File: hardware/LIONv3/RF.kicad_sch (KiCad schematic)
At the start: 17 parts, among them U5 E80-900M2213S, U6 INA226AIDGSR, U7 XL-1608UBC-04, U8 W25Q16JVSSIQTR

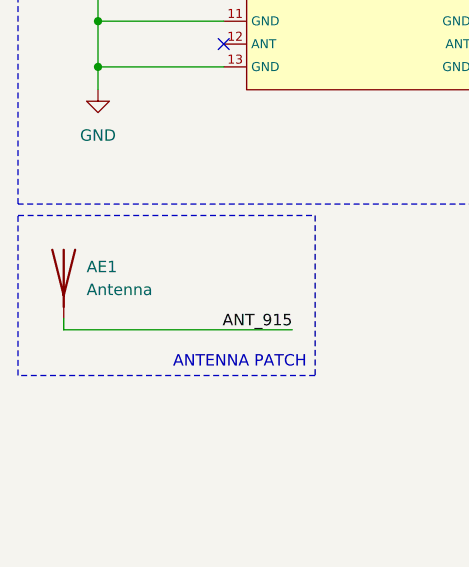
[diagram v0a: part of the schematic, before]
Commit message: feat(hardware): organize repo structure
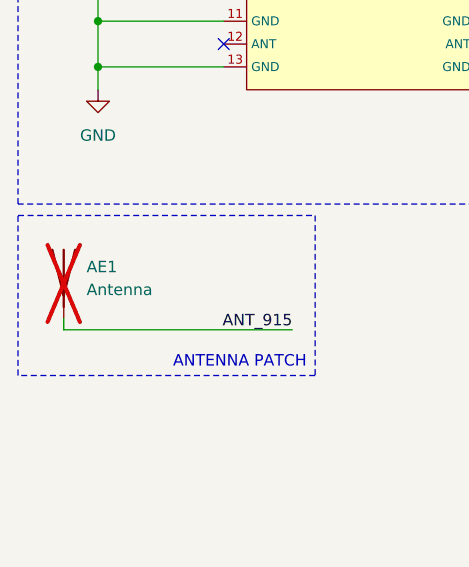
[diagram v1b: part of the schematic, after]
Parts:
- AE1: now not fitted
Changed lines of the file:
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@@
 		(unit 1)
 		(body_style 1)
-		(exclude_from_sim no)
+		(exclude_from_sim yes)
 		(in_bom no)
-		(on_board yes)
+		(on_board no)
 		(in_pos_files no)
-		(dnp no)
+		(dnp yes)
 		(fields_autoplaced yes)
 		(property "Reference" "AE1"

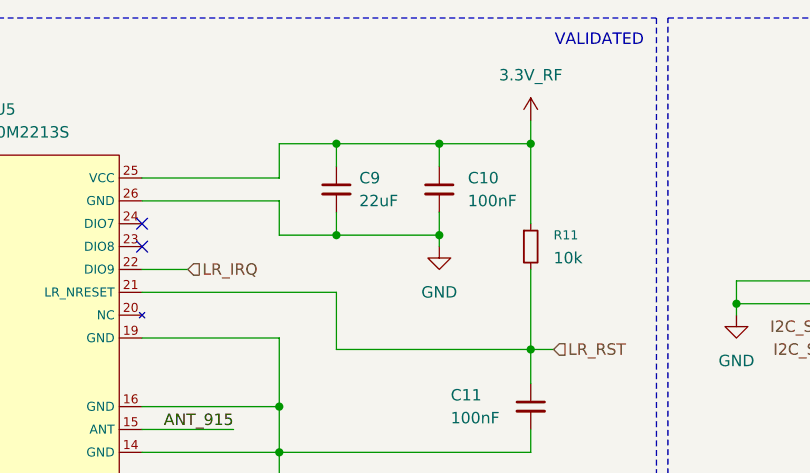
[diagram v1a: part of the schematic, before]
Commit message: Add TVS diode protection (ESD9B3.3ST5G)
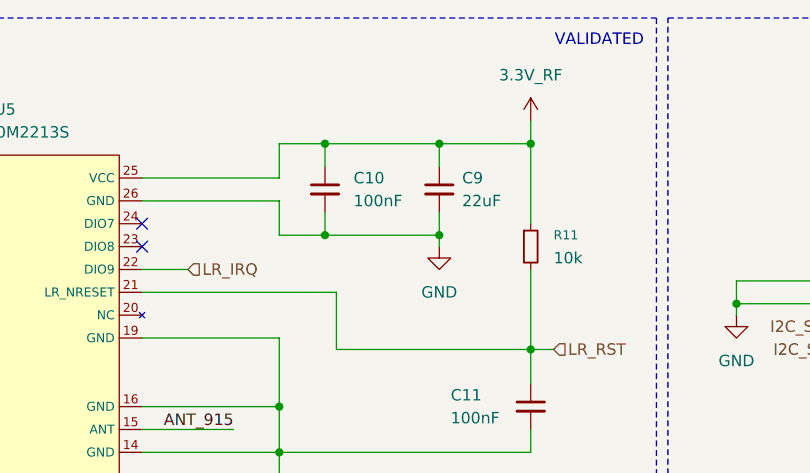
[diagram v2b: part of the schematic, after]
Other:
- moved on the sheet: C10, C9
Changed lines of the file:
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@@
 	)
 	(junction
-		(at 88.9 27.94)
-		(diameter 0)
-		(color 0 0 0 0)
-	)
-	(junction
 		(at 110.49 27.94)
 		(diameter 0)
@@
 	)
 	(junction
-		(at 88.9 38.1)
+		(at 87.63 27.94)
 		(diameter 0)
 		(color 0 0 0 0)
@@
 	)
 	(junction
-		(at 22.86 52.07)
+		(at 100.33 27.94)
 		(diameter 0)
 		(color 0 0 0 0)
 	)
 	(junction
-		(at 82.55 62.23)
+		(at 22.86 52.07)
 		(diameter 0)
 		(color 0 0 0 0)
 	)
 	(junction
-		(at 110.49 50.8)
+		(at 82.55 62.23)
 		(diameter 0)
 		(color 0 0 0 0)
 	)
 	(junction
-		(at 31.75 34.29)
+		(at 110.49 50.8)
 		(diameter 0)
 		(color 0 0 0 0)
 	)
 	(junction
-		(at 100.33 27.94)
+		(at 31.75 34.29)
 		(diameter 0)
 		(color 0 0 0 0)
@@
 	)
 	(junction
-		(at 182.88 33.02)
+		(at 87.63 38.1)
 		(diameter 0)
 		(color 0 0 0 0)
 	)
 	(junction
-		(at 22.86 57.15)
+		(at 182.88 33.02)
 		(diameter 0)
 		(color 0 0 0 0)
 	)
 	(junction
-		(at 100.33 38.1)
+		(at 22.86 57.15)
 		(diameter 0)
 		(color 0 0 0 0)
@@
 	)
 	(junction
+		(at 100.33 38.1)
+		(diameter 0)
+		(color 0 0 0 0)
+	)
+	(junction
 		(at 82.55 57.15)
 		(diameter 0)
@@
 	(wire
 		(pts
-			(xy 88.9 27.94) (xy 88.9 30.48)
+			(xy 100.33 27.94) (xy 100.33 30.48)
 		)
 		(stroke
@@
 	(wire
 		(pts
-			(xy 82.55 57.15) (xy 82.55 62.23)
+			(xy 87.63 38.1) (xy 100.33 38.1)
 		)
 		(stroke
@@
 	(wire
 		(pts
-			(xy 100.33 30.48) (xy 100.33 27.94)
+			(xy 82.55 57.15) (xy 82.55 62.23)
 		)
 		(stroke
@@
 	(wire
 		(pts
-			(xy 22.86 52.07) (xy 36.83 52.07)
+			(xy 87.63 30.48) (xy 87.63 27.94)
 		)
 		(stroke
@@
 	(wire
 		(pts
-			(xy 29.21 41.91) (xy 36.83 41.91)
+			(xy 22.86 52.07) (xy 36.83 52.07)
 		)
 		(stroke
@@
 	(wire
 		(pts
-			(xy 100.33 38.1) (xy 88.9 38.1)
+			(xy 29.21 41.91) (xy 36.83 41.91)
 		)
 		(stroke
@@
 	(wire
 		(pts
-			(xy 88.9 35.56) (xy 88.9 38.1)
+			(xy 100.33 35.56) (xy 100.33 38.1)
 		)
 		(stroke
@@
 	(wire
 		(pts
+			(xy 87.63 27.94) (xy 100.33 27.94)
+		)
+		(stroke
+			(width 0)
+			(type default)
+		)
+	)
+	(wire
+		(pts
 			(xy 67.31 49.53) (xy 82.55 49.53)
 		)
@@
 	(wire
 		(pts
-			(xy 82.55 27.94) (xy 110.49 27.94)
+			(xy 82.55 27.94) (xy 87.63 27.94)
 		)
 		(stroke
@@
 	(wire
 		(pts
-			(xy 88.9 38.1) (xy 82.55 38.1)
+			(xy 82.55 38.1) (xy 87.63 38.1)
 		)
 		(stroke
@@
 	(wire
 		(pts
+			(xy 100.33 27.94) (xy 110.49 27.94)
+		)
+		(stroke
+			(width 0)
+			(type default)
+		)
+	)
+	(wire
+		(pts
 			(xy 273.05 107.95) (xy 273.05 109.22)
 		)
@@
 	(wire
 		(pts
-			(xy 100.33 35.56) (xy 100.33 38.1)
+			(xy 87.63 35.56) (xy 87.63 38.1)
 		)
 		(stroke
@@
 	(symbol
 		(lib_id "Device:C_Small")
-		(at 88.9 33.02 0)
+		(at 100.33 33.02 0)
 		(unit 1)
 		(body_style 1)
@@
 		(fields_autoplaced yes)
 		(property "Reference" "C9"
-			(at 91.44 31.7562 0)
+			(at 102.87 31.7562 0)
 			(show_name no)
 			(do_not_autoplace no)
@@
 		)
 		(property "Value" "22uF"
-			(at 91.44 34.2962 0)
+			(at 102.87 34.2962 0)
 			(show_name no)
 			(do_not_autoplace no)
@@
 		)
 		(property "Footprint" "Capacitor_SMD:C_0805_2012Metric"
-			(at 88.9 33.02 0)
+			(at 100.33 33.02 0)
 			(hide yes)
 			(show_name no)
@@
 		)
 		(property "Datasheet" ""
-			(at 88.9 33.02 0)
+			(at 100.33 33.02 0)
 			(hide yes)
 			(show_name no)
@@
 		)
 		(property "Description" "Unpolarized capacitor, small symbol"
-			(at 88.9 33.02 0)
+			(at 100.33 33.02 0)
 			(hide yes)
 			(show_name no)
@@
 		)
 		(property "LCSC" "C45783"
-			(at 88.9 33.02 0)
+			(at 100.33 33.02 0)
 			(hide yes)
 			(show_name no)
@@
 	(symbol
 		(lib_id "Device:C_Small")
-		(at 100.33 33.02 0)
+		(at 87.63 33.02 0)
 		(unit 1)
 		(body_style 1)
@@
 		(fields_autoplaced yes)
 		(property "Reference" "C10"
-			(at 103.505 31.7562 0)
+			(at 90.805 31.7562 0)
 			(show_name no)
 			(do_not_autoplace no)
@@
 		)
 		(property "Value" "100nF"
-			(at 103.505 34.2962 0)
+			(at 90.805 34.2962 0)
 			(show_name no)
 			(do_not_autoplace no)
@@
 		)
 		(property "Footprint" "Capacitor_SMD:C_0402_1005Metric"
-			(at 100.33 33.02 0)
+			(at 87.63 33.02 0)
 			(hide yes)
 			(show_name no)
@@
 		)
 		(property "Datasheet" ""
-			(at 100.33 33.02 0)
+			(at 87.63 33.02 0)
 			(hide yes)
 			(show_name no)
@@
 		)
 		(property "Description" "Unpolarized capacitor, small symbol"
-			(at 100.33 33.02 0)
+			(at 87.63 33.02 0)
 			(hide yes)
 			(show_name no)
@@
 		)
 		(property "LCSC" "C307331"
-			(at 100.33 33.02 0)
+			(at 87.63 33.02 0)
 			(hide yes)
 			(show_name no)

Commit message: feat(hardware): improves LED series currents
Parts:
- R14: value 68 -> 1k
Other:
- note added: "BLUE RX/TX@3.4mA"
- note removed: "BLUE RX/TX"
- note removed: "VALIDATED"
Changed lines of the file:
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@@
 		(comment 3 "2026-08-12")
 	)
-	(text "BLUE RX/TX\n"
+	(text "BLUE RX/TX@3.4mA"
 		(exclude_from_sim no)
 		(at 236.22 43.18 0)
@@
 		)
 	)
-	(text "VALIDATED"
-		(exclude_from_sim no)
-		(at 118.11 16.51 0)
-		(effects
-			(font
-				(size 1.27 1.27)
-			)
-		)
-	)
-	(text "VALIDATED"
-		(exclude_from_sim no)
-		(at 276.86 81.28 0)
-		(effects
-			(font
-				(size 1.27 1.27)
-			)
-		)
-	)
-	(text "VALIDATED"
-		(exclude_from_sim no)
-		(at 204.47 16.51 0)
-		(effects
-			(font
-				(size 1.27 1.27)
-			)
-		)
-	)
-	(text "VALIDATED"
-		(exclude_from_sim no)
-		(at 276.86 16.51 0)
-		(effects
-			(font
-				(size 1.27 1.27)
-			)
-		)
-	)
 	(text_box "MEMORY"
 		(exclude_from_sim no)
@@
 			)
 		)
-		(property "Value" "68"
+		(property "Value" "1k"
 			(at 251.46 35.56 90)
 			(show_name no)
@@
 			)
 		)
-		(property "Datasheet" "https://atta.szlcsc.com/upload/public/pdf/source/20210617/C2837377_50FC585D376FE0CDA016E524346528FF.pdf"
+		(property "Datasheet" "https://www.lcsc.com/datasheet/C965807.pdf"
 			(at 233.934 37.973 0)
 			(hide yes)

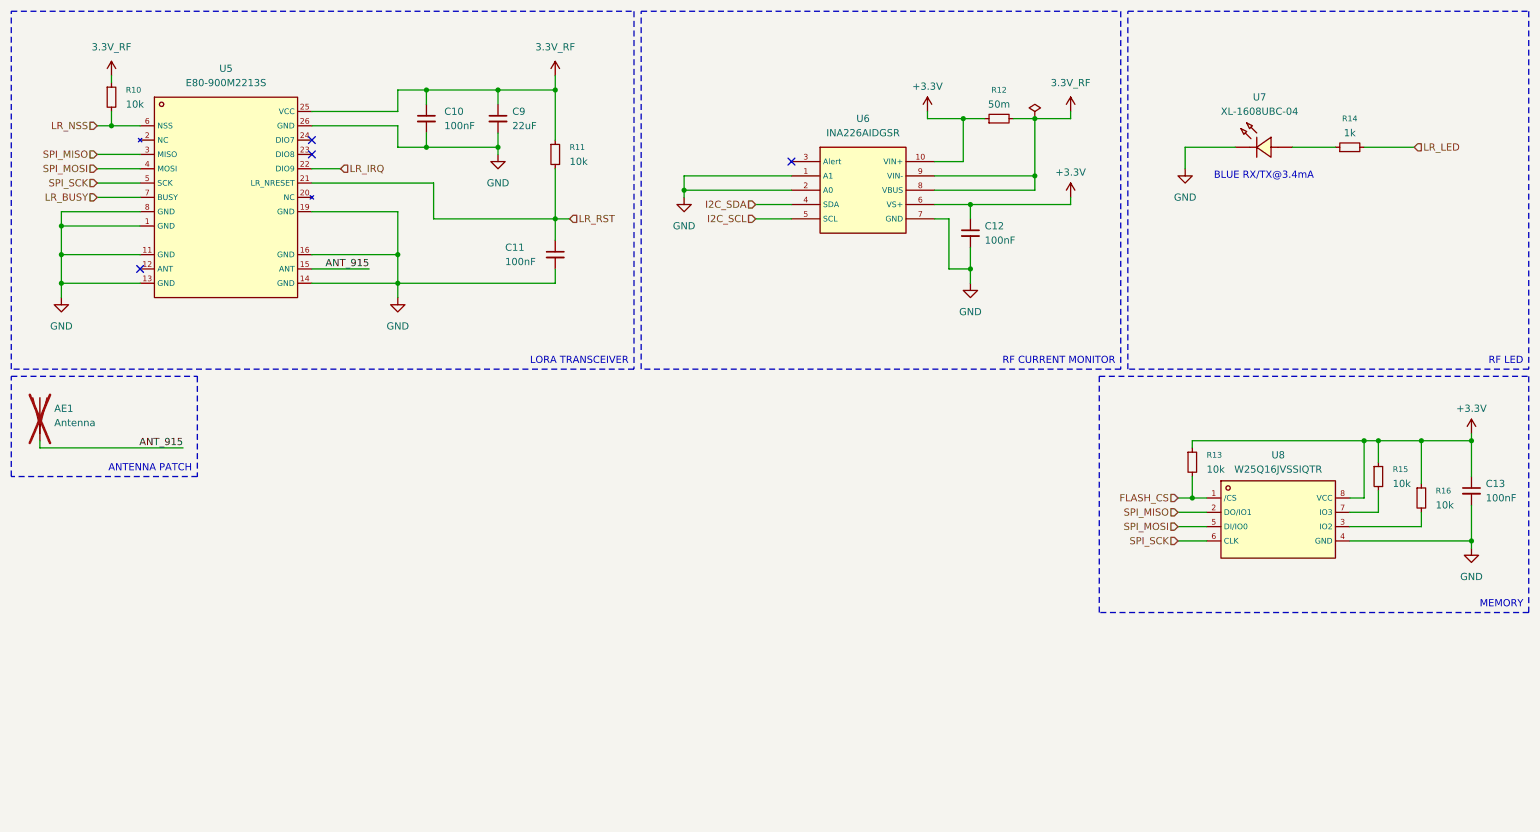
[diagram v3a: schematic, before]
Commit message: feat(hardware): change SPI terminology (new OSHWA naming conventions)
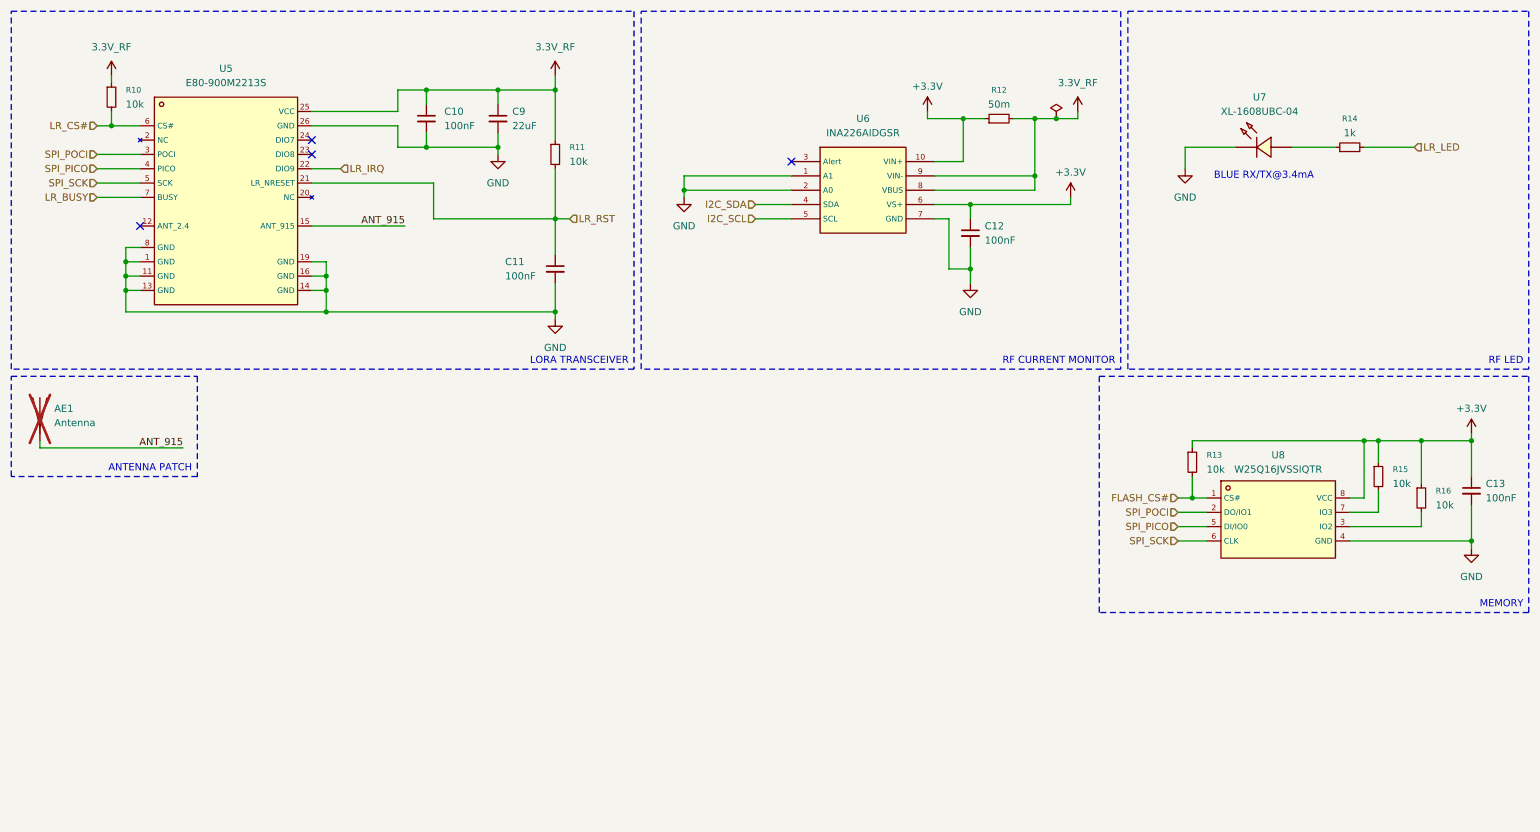
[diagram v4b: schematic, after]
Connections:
- net FLASH_CS renamed FLASH_CS#
- net LR_NSS renamed LR_CS#
- net SPI_MISO renamed SPI_POCI
- net SPI_MOSI renamed SPI_PICO
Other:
- moved on the sheet: C11, U5

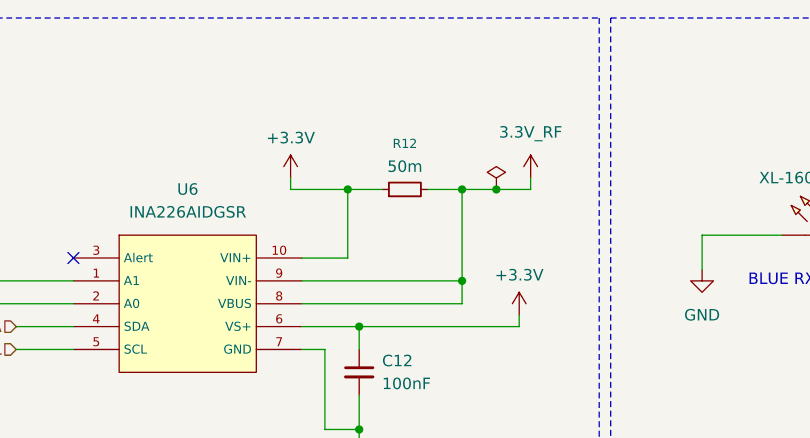
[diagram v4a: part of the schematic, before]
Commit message: feat(hardware): add shunt resistor rating to schematic
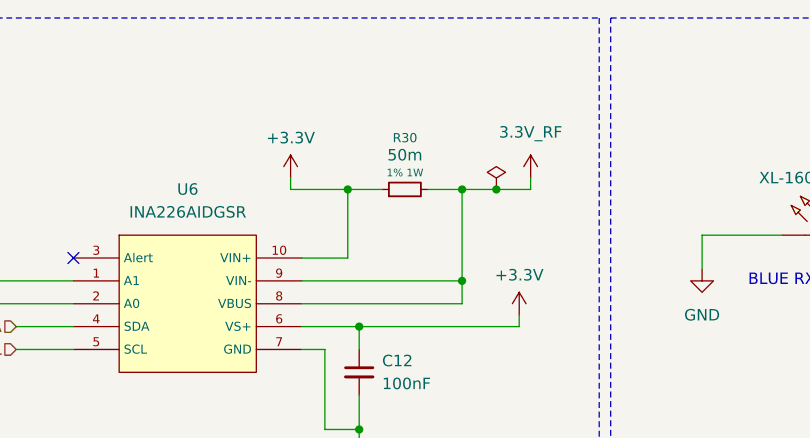
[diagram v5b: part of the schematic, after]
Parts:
- removed R12: 50m, LIONv3-Footprints:R1206, symbol Device:R_Small
- added R30: 50m, LIONv3-Footprints:R1206, symbol Device:R_Small
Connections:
- net +3.3V: now also R30.1
- net 3.3V_RF: now also R30.2
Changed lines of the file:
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@@
-	)
-	(symbol
-		(lib_id "Device:R_Small")
-		(at 189.23 33.02 90)
-		(unit 1)
-		(body_style 1)
-		(exclude_from_sim no)
-		(in_bom yes)
-		(on_board yes)
-		(in_pos_files yes)
-		(dnp no)
-		(fields_autoplaced yes)
-		(property "Reference" "R12"
-			(at 189.23 27.94 90)
-			(show_name no)
-			(do_not_autoplace no)
-			(effects
-				(font
-					(size 1.016 1.016)
-				)
-			)
-		)
-		(property "Value" "50m"
-			(at 189.23 30.48 90)
-			(show_name no)
-			(do_not_autoplace no)
-			(effects
-				(font
-					(size 1.27 1.27)
-				)
-			)
-		)
-		(property "Footprint" "LIONv3-Footprints:R1206"
-			(at 189.23 33.02 0)
-			(hide yes)
-			(show_name no)
-			(do_not_autoplace no)
-			(effects
-				(font
-					(size 1.27 1.27)
-				)
-			)
-		)
-		(property "Datasheet" "https://www.lcsc.com/datasheet/C20608719.pdf"
-			(at 189.23 33.02 0)
-			(hide yes)
-			(show_name no)
-			(do_not_autoplace no)
-			(effects
-				(font
-					(size 1.27 1.27)
-				)
-			)
-		)
-		(property "Description" "Resistor, small symbol"
-			(at 189.23 33.02 0)
-			(hide yes)
-			(show_name no)
-			(do_not_autoplace no)
-			(effects
-				(font
-					(size 1.27 1.27)
-				)
-			)
-		)
-		(property "LCSC" "C20608719"
-			(at 189.23 33.02 90)
-			(hide yes)
-			(show_name no)
-			(do_not_autoplace no)
-			(effects
-				(font
-					(size 1.27 1.27)
-				)
-			)
-		)
-		(pin "2"
-		)
-		(pin "1"
-		)
-		(instances
-			(project "LIONv3"
-				(path "/3cc9e06f-00d0-4bec-822f-2e156022ced4/d6030e6b-69d2-4923-80e2-2aab4b335fec"
-					(reference "R12")
-					(unit 1)
-				)
-			)
-		)
 	)
 	(symbol
@@
 					(unit 1)
 				)
+			)
+		)
+	)
+	(symbol
+		(lib_id "Device:R_Small")
+		(at 189.23 33.02 90)
+		(unit 1)
+		(body_style 1)
+		(exclude_from_sim no)
+		(in_bom yes)
+		(on_board yes)
+		(in_pos_files yes)
+		(dnp no)
+		(property "Reference" "R30"
+			(at 189.2392 27.3041 90)
+			(show_name no)
+			(do_not_autoplace no)
+			(effects
+				(font
+					(size 1.016 1.016)
+				)
+			)
+		)
+		(property "Value" "50m"
+			(at 189.23 29.21 90)
+			(show_name no)
+			(do_not_autoplace no)
+			(effects
+				(font
+					(size 1.27 1.27)
+				)
+			)
+		)
+		(property "Footprint" "LIONv3-Footprints:R1206"
+			(at 189.23 33.02 0)
+			(hide yes)
+			(show_name no)
+			(do_not_autoplace no)
+			(effects
+				(font
+					(size 1.27 1.27)
+				)
+			)
+		)
+		(property "Datasheet" "https://www.lcsc.com/datasheet/C20608719.pdf"
+			(at 189.23 33.02 0)
+			(hide yes)
+			(show_name no)
+			(do_not_autoplace no)
+			(effects
+				(font
+					(size 1.27 1.27)
+				)
+			)
+		)
+		(property "Description" "Resistor, small symbol"
+			(at 189.23 33.02 0)
+			(hide yes)
+			(show_name no)
+			(do_not_autoplace no)
+			(effects
+				(font
+					(size 1.27 1.27)
+				)
+			)
+		)
+		(property "LCSC" "C20608719"
+			(at 189.23 33.02 90)
+			(hide yes)
+			(show_name no)
+			(do_not_autoplace no)
+			(effects
+				(font
+					(size 1.27 1.27)
+				)
+			)
+		)
+		(property "Tolerance" "1%"
+			(at 189.23 33.02 90)
+			(hide yes)
+			(show_name no)
+			(do_not_autoplace no)
+			(effects
+				(font
+					(size 1.27 1.27)
+				)
+			)
+		)
+		(property "Rated_Power" "1W"
+			(at 189.23 33.02 90)
+			(hide yes)
+			(show_name no)
+			(do_not_autoplace no)
+			(effects
+				(font
+					(size 1.27 1.27)
+				)
+			)
+		)
+		(property "Rating" "${Tolerance} ${Rated_Power}"
+			(at 189.2392 31.1677 90)
+			(show_name no)
+			(do_not_autoplace no)
+			(effects
+				(font
+					(size 0.8467 0.8467)
+				)
+			)
+		)
+		(pin "2"
+		)
+		(pin "1"
+		)
+		(instances
+			(project "LIONv3"
+				(path "/3cc9e06f-00d0-4bec-822f-2e156022ced4/d6030e6b-69d2-4923-80e2-2aab4b335fec"
+					(reference "R30")
+					(unit 1)
+				)
